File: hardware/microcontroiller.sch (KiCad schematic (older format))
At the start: 16 parts, among them J100 Conn_01x03, J2 Conn_02x03_Odd_Even, J3 USB_A, SW1 RESET Switch, U1 STM32L4Q5xx, Y1 32.768kHz

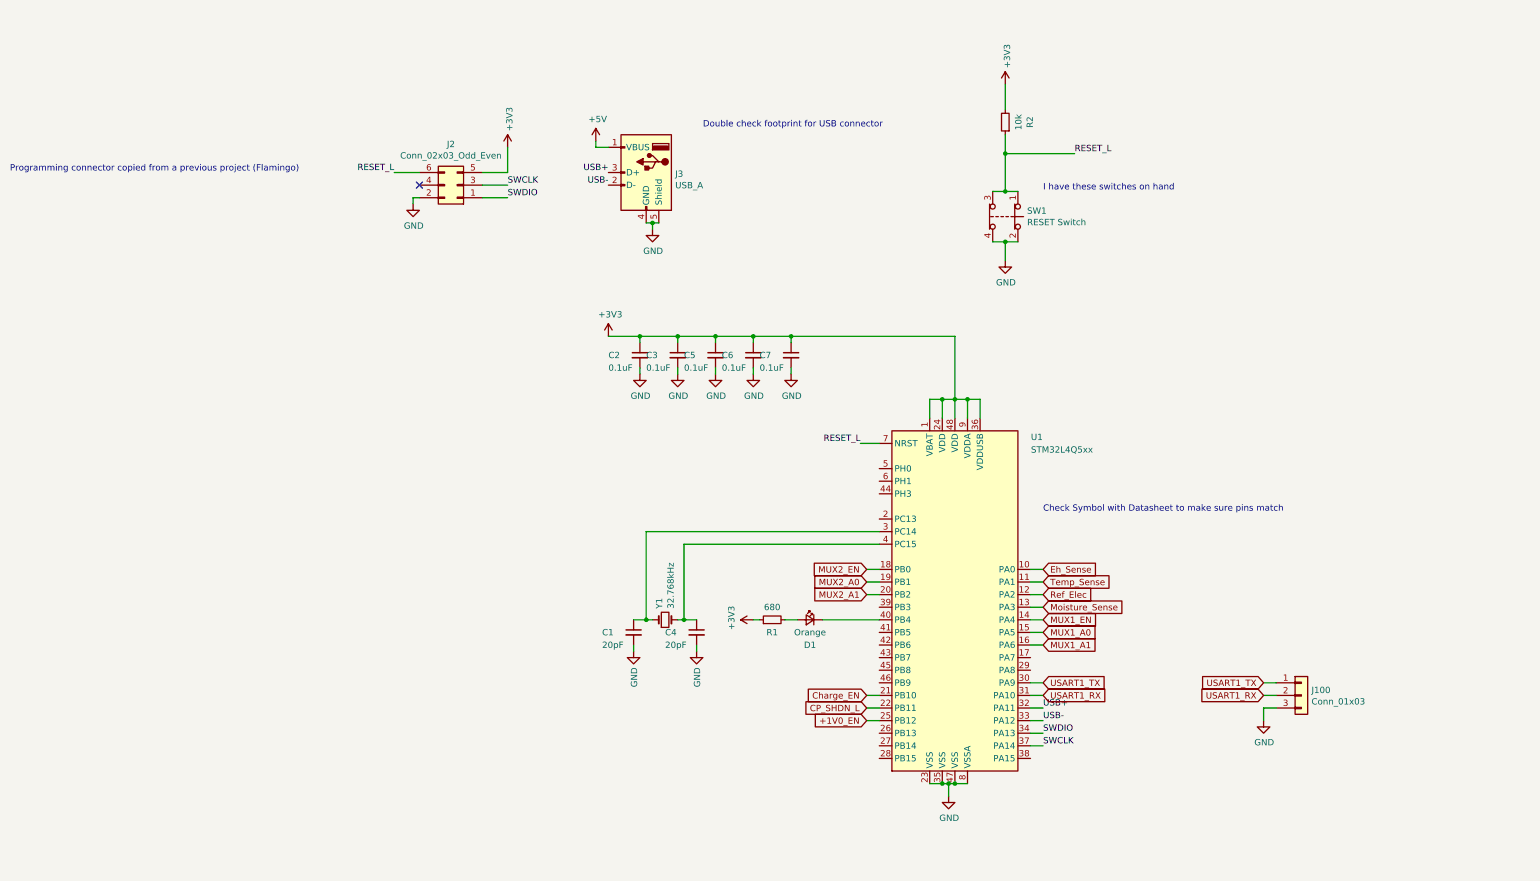
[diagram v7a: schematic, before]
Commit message: Updated footprint and added decoupling caps
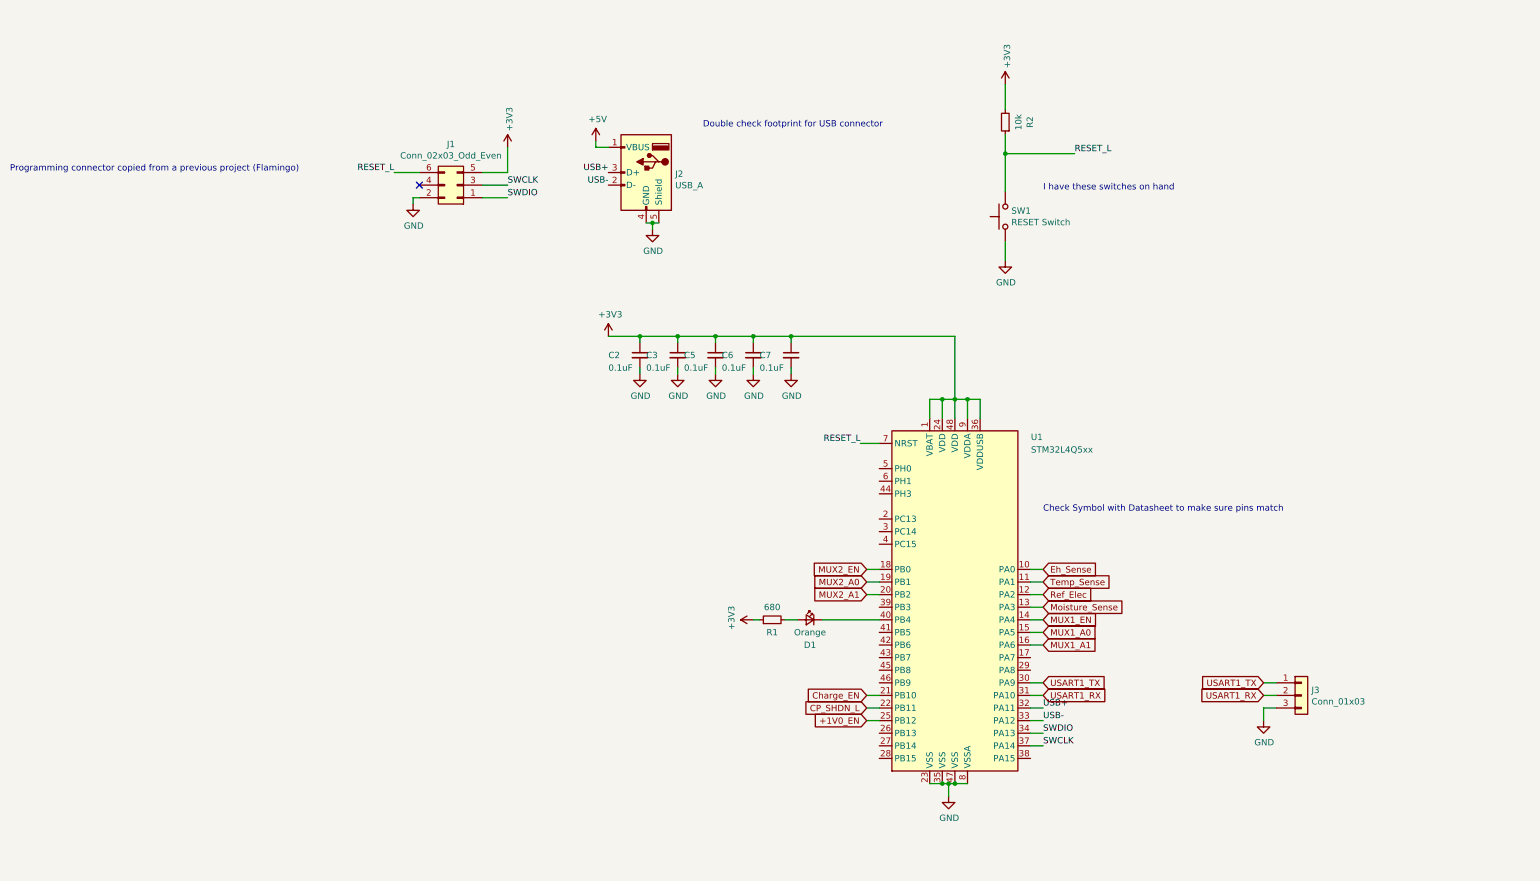
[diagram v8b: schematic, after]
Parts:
- removed C1, C4: 20pF, Capacitor_SMD:C_0603_1608Metric_Pad1.08x0.95mm_HandSolder, symbol mallard-rescue:C_Small-Device
- removed SW1: RESET Switch, Button_Switch_SMD:SW_SPST_B3U-1000P, symbol mallard-rescue:SW_Push_Open_Dual-Switch
- removed Y1: 32.768kHz, symbol mallard-rescue:Crystal_Small-Device
- added SW1: RESET Switch, Button_Switch_SMD:SW_SPST_B3U-1000P, symbol Switch:SW_Push
- renumbered J2 to J1, J3 to J2, J100 to J3
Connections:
- net GND: now also SW1.1
- net RESET_L: now also SW1.2
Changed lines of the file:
@@
 $Descr A4 11693 8268
 encoding utf-8
-Sheet 1 1
+Sheet 2 4
 Title ""
 Date ""
@@
 $EndDescr
 $Comp
-L mallard-rescue:+3V3-power #PWR07
+L mallard-rescue:+3V3-power #PWR04
 U 1 1 6157176B
 P 3200 3100
-F 0 "#PWR07" H 3200 2950 50  0001 C CNN
+F 0 "#PWR04" H 3200 2950 50  0001 C CNN
 F 1 "+3V3" H 3215 3273 50  0000 C CNN
 F 2 "" H 3200 3100 50  0001 C CNN
@@
 	6350 1300 6350 1100
 $Comp
-L mallard-rescue:+3V3-power #PWR018
+L mallard-rescue:+3V3-power #PWR015
 U 1 1 6157E7E5
 P 6350 1100
-F 0 "#PWR018" H 6350 950 50  0001 C CNN
+F 0 "#PWR015" H 6350 950 50  0001 C CNN
 F 1 "+3V3" V 6365 1228 50  0000 L CNN
 F 2 "" H 6350 1100 50  0001 C CNN
@@
 $EndComp
 $Comp
-L mallard-rescue:GND-power #PWR019
+L mallard-rescue:GND-power #PWR016
 U 1 1 615824DA
 P 6350 2500
-F 0 "#PWR019" H 6350 2250 50  0001 C CNN
+F 0 "#PWR016" H 6350 2250 50  0001 C CNN
 F 1 "GND" H 6355 2327 50  0000 C CNN
 F 2 "" H 6350 2500 50  0001 C CNN
@@
 Wire Wire Line
 	5350 3950 5200 3950
-$Comp
-L mallard-rescue:Crystal_Small-Device Y1
-U 1 1 6158BC98
-P 3650 5350
-F 0 "Y1" V 3604 5438 50  0000 L CNN
-F 1 "32.768kHz" V 3695 5438 50  0000 L CNN
-F 2 "" H 3650 5350 50  0001 C CNN
-F 3 "~" H 3650 5350 50  0001 C CNN
-	1    3650 5350
-	1    0    0    -1
-$EndComp
-$Comp
-L mallard-rescue:C_Small-Device C1
-U 1 1 6158E0B8
-P 3400 5450
-F 0 "C1" H 3150 5450 50  0000 L CNN
-F 1 "20pF" H 3150 5350 50  0000 L CNN
-F 2 "Capacitor_SMD:C_0603_1608Metric_Pad1.08x0.95mm_HandSolder" H 3400 5450 50  0001 C CNN
-F 3 "https://content.kemet.com/datasheets/KEM_C1007_X8R_ULTRA_150C_SMD.pdf" H 3400 5450 50  0001 C CNN
-F 4 "399-C0603C200G4HAC7867CT-ND" H 3400 5450 50  0001 C CNN "Digikey"
-	1    3400 5450
-	1    0    0    -1
-$EndComp
-$Comp
-L mallard-rescue:GND-power #PWR08
-U 1 1 6158FD84
-P 3400 5600
-F 0 "#PWR08" H 3400 5350 50  0001 C CNN
-F 1 "GND" V 3405 5472 50  0000 R CNN
-F 2 "" H 3400 5600 50  0001 C CNN
-F 3 "" H 3400 5600 50  0001 C CNN
-	1    3400 5600
-	1    0    0    -1
-$EndComp
 Text Notes 6650 4500 0    50   ~ 0
 Check Symbol with Datasheet to make sure pins match
@@
 Connection ~ 5900 6650
 $Comp
-L mallard-rescue:GND-power #PWR017
+L mallard-rescue:GND-power #PWR014
 U 1 1 616159A6
 P 5900 6750
-F 0 "#PWR017" H 5900 6500 50  0001 C CNN
+F 0 "#PWR014" H 5900 6500 50  0001 C CNN
 F 1 "GND" H 5905 6577 50  0000 C CNN
 F 2 "" H 5900 6750 50  0001 C CNN
@@
 $EndComp
 $Comp
-L mallard-rescue:USB_A-Connector J?
+L mallard-rescue:USB_A-Connector J2
 U 1 1 6161D470
 P 3500 1800
-AR Path="/6161D470" Ref="J?"  Part="1"
-AR Path="/60B3FDDE/6161D470" Ref="J3"  Part="1"
-F 0 "J3" H 3270 1789 50  0000 R CNN
+AR Path="/6161D470" Ref="J2"  Part="1"
+AR Path="/60B3FDDE/6161D470" Ref="J?"  Part="1"
+F 0 "J?" H 3270 1789 50  0000 R CNN
 F 1 "USB_A" H 3270 1698 50  0000 R CNN
 F 2 "Connector_USB:USB3_A_Molex_48393-001" H 3650 1750 50  0001 C CNN
@@
 $EndComp
 $Comp
-L mallard-rescue:+5V-power #PWR06
+L mallard-rescue:+5V-power #PWR03
 U 1 1 6162177A
 P 3100 1550
-F 0 "#PWR06" H 3100 1400 50  0001 C CNN
+F 0 "#PWR03" H 3100 1400 50  0001 C CNN
 F 1 "+5V" H 3115 1723 50  0000 C CNN
 F 2 "" H 3100 1550 50  0001 C CNN
@@
 USB-
 $Comp
-L mallard-rescue:GND-power #PWR010
+L mallard-rescue:GND-power #PWR07
 U 1 1 6162345E
 P 3550 2250
-F 0 "#PWR010" H 3550 2000 50  0001 C CNN
+F 0 "#PWR07" H 3550 2000 50  0001 C CNN
 F 1 "GND" H 3555 2077 50  0000 C CNN
 F 2 "" H 3550 2250 50  0001 C CNN
@@
 Wire Wire Line
 	3550 2200 3500 2200
-$Comp
-L mallard-rescue:SW_Push_Open_Dual-Switch SW1
-U 1 1 6162FC27
-P 6450 2150
-F 0 "SW1" V 6404 2223 50  0000 L CNN
-F 1 "RESET Switch" V 6495 2223 50  0000 L CNN
-F 2 "Button_Switch_SMD:SW_SPST_B3U-1000P" H 6450 2350 50  0001 C CNN
-F 3 "https://omronfs.omron.com/en_US/ecb/products/pdf/en-b3u.pdf" H 6450 2350 50  0001 C CNN
-F 4 "SW1020CT-ND" H 6450 2150 50  0001 C CNN "Digikey"
-	1    6450 2150
-	0    1    1    0
-$EndComp
-Wire Wire Line
-	6250 2350 6350 2350
-Connection ~ 6350 2350
-Wire Wire Line
-	6350 2350 6450 2350
 Wire Wire Line
 	6350 2350 6350 2500
-Wire Wire Line
-	6250 1950 6350 1950
-Connection ~ 6350 1950
-Wire Wire Line
-	6350 1950 6450 1950
 $Comp
 L mallard-rescue:LED_Small-Device D1
@@
 	4600 5350 4700 5350
 $Comp
-L mallard-rescue:+3V3-power #PWR015
+L mallard-rescue:+3V3-power #PWR012
 U 1 1 61652B46
 P 4350 5350
-F 0 "#PWR015" H 4350 5200 50  0001 C CNN
+F 0 "#PWR012" H 4350 5200 50  0001 C CNN
 F 1 "+3V3" H 4365 5523 50  0000 C CNN
 F 2 "" H 4350 5350 50  0001 C CNN
@@
 	5250 6150 5350 6150
 $Comp
-L mallard-rescue:GND-power #PWR09
+L mallard-rescue:GND-power #PWR06
 U 1 1 615C81D2
 P 3450 3400
-F 0 "#PWR09" H 3450 3150 50  0001 C CNN
+F 0 "#PWR06" H 3450 3150 50  0001 C CNN
 F 1 "GND" H 3455 3227 50  0000 C CNN
 F 2 "" H 3450 3400 50  0001 C CNN
@@
 Connection ~ 4050 3100
 $Comp
-L mallard-rescue:GND-power #PWR011
+L mallard-rescue:GND-power #PWR08
 U 1 1 61A5AA42
 P 3750 3400
-F 0 "#PWR011" H 3750 3150 50  0001 C CNN
+F 0 "#PWR08" H 3750 3150 50  0001 C CNN
 F 1 "GND" H 3755 3227 50  0000 C CNN
 F 2 "" H 3750 3400 50  0001 C CNN
@@
 $EndComp
 $Comp
-L mallard-rescue:GND-power #PWR013
+L mallard-rescue:GND-power #PWR010
 U 1 1 61A5C967
 P 4050 3400
-F 0 "#PWR013" H 4050 3150 50  0001 C CNN
+F 0 "#PWR010" H 4050 3150 50  0001 C CNN
 F 1 "GND" H 4055 3227 50  0000 C CNN
 F 2 "" H 4050 3400 50  0001 C CNN
@@
 $EndComp
 $Comp
-L mallard-rescue:GND-power #PWR014
+L mallard-rescue:GND-power #PWR011
 U 1 1 61A5E793
 P 4350 3400
-F 0 "#PWR014" H 4350 3150 50  0001 C CNN
+F 0 "#PWR011" H 4350 3150 50  0001 C CNN
 F 1 "GND" H 4355 3227 50  0000 C CNN
 F 2 "" H 4350 3400 50  0001 C CNN
@@
 $EndComp
 $Comp
-L mallard-rescue:GND-power #PWR016
+L mallard-rescue:GND-power #PWR013
 U 1 1 61A60A8A
 P 4650 3400
-F 0 "#PWR016" H 4650 3150 50  0001 C CNN
+F 0 "#PWR013" H 4650 3150 50  0001 C CNN
 F 1 "GND" H 4655 3227 50  0000 C CNN
 F 2 "" H 4650 3400 50  0001 C CNN
@@
 Connection ~ 6050 3600
 $Comp
-L mallard-rescue:C_Small-Device C4
-U 1 1 61A825EB
-P 3900 5450
-F 0 "C4" H 3650 5450 50  0000 L CNN
-F 1 "20pF" H 3650 5350 50  0000 L CNN
-F 2 "Capacitor_SMD:C_0603_1608Metric_Pad1.08x0.95mm_HandSolder" H 3900 5450 50  0001 C CNN
-F 3 "https://content.kemet.com/datasheets/KEM_C1007_X8R_ULTRA_150C_SMD.pdf" H 3900 5450 50  0001 C CNN
-F 4 "399-C0603C200G4HAC7867CT-ND" H 3900 5450 50  0001 C CNN "Digikey"
-	1    3900 5450
-	1    0    0    -1
-$EndComp
-$Comp
 L mallard-rescue:C_Small-Device C3
 U 1 1 61A86DBF
@@
 Text Notes 3950 1450 0    50   ~ 0
 Double check footprint for USB connector
-$Comp
-L mallard-rescue:GND-power #PWR012
-U 1 1 618D755A
-P 3900 5600
-F 0 "#PWR012" H 3900 5350 50  0001 C CNN
-F 1 "GND" V 3905 5472 50  0000 R CNN
-F 2 "" H 3900 5600 50  0001 C CNN
-F 3 "" H 3900 5600 50  0001 C CNN
-	1    3900 5600
-	1    0    0    -1
-$EndComp
-Wire Wire Line
-	3400 5600 3400 5550
-Wire Wire Line
-	3900 5600 3900 5550
-Wire Wire Line
-	3400 5350 3500 5350
-Wire Wire Line
-	3900 5350 3800 5350
-Wire Wire Line
-	3500 5350 3500 4650
-Wire Wire Line
-	3500 4650 5350 4650
-Connection ~ 3500 5350
-Wire Wire Line
-	3500 5350 3550 5350
-Wire Wire Line
-	3800 5350 3800 4750
-Wire Wire Line
-	3800 4750 5350 4750
-Connection ~ 3800 5350
-Wire Wire Line
-	3800 5350 3750 5350
 Wire Wire Line
 	6350 1500 6350 1650
@@
 Programming connector copied from a previous project (Flamingo)
 $Comp
-L Connector_Generic:Conn_02x03_Odd_Even J2
+L Connector_Generic:Conn_02x03_Odd_Even J1
 U 1 1 61EC204C
 P 2000 1900
-F 0 "J2" H 2050 1575 50  0000 C CNN
+F 0 "J1" H 2050 1575 50  0000 C CNN
 F 1 "Conn_02x03_Odd_Even" H 2050 1666 50  0000 C CNN
 F 2 "Connector_PinHeader_1.27mm:PinHeader_2x03_P1.27mm_Vertical" H 2000 1900 50  0001 C CNN
@@
 	1650 2000 1650 2050
 $Comp
-L mallard-rescue:GND-power #PWR04
+L mallard-rescue:GND-power #PWR01
 U 1 1 61ECF0E0
 P 1650 2050
-F 0 "#PWR04" H 1650 1800 50  0001 C CNN
+F 0 "#PWR01" H 1650 1800 50  0001 C CNN
 F 1 "GND" H 1655 1877 50  0000 C CNN
 F 2 "" H 1650 2050 50  0001 C CNN
@@
 $EndComp
 $Comp
-L mallard-rescue:+3V3-power #PWR05
+L mallard-rescue:+3V3-power #PWR02
 U 1 1 61ED1EE0
 P 2400 1600
-F 0 "#PWR05" H 2400 1450 50  0001 C CNN
+F 0 "#PWR02" H 2400 1450 50  0001 C CNN
 F 1 "+3V3" V 2415 1728 50  0000 L CNN
 F 2 "" H 2400 1600 50  0001 C CNN
@@
 	8500 5850 8400 5850
 $Comp
-L Connector_Generic:Conn_01x03 J100
+L Connector_Generic:Conn_01x03 J3
 U 1 1 61EA675F
 P 8700 5950
-F 0 "J100" H 8780 5992 50  0000 L CNN
+F 0 "J3" H 8780 5992 50  0000 L CNN
 F 1 "Conn_01x03" H 8780 5901 50  0000 L CNN
 F 2 "Connector_PinHeader_2.54mm:PinHeader_1x03_P2.54mm_Vertical_SMD_Pin1Right" H 8700 5950 50  0001 C CNN
@@
 	8400 6050 8400 6150
 $Comp
-L mallard-rescue:GND-power #PWR?
+L mallard-rescue:GND-power #PWR017
 U 1 1 61EAAB16
 P 8400 6150
-F 0 "#PWR?" H 8400 5900 50  0001 C CNN
+F 0 "#PWR017" H 8400 5900 50  0001 C CNN
 F 1 "GND" H 8405 5977 50  0000 C CNN
 F 2 "" H 8400 6150 50  0001 C CNN
@@
 Wire Wire Line
 	8500 6050 8400 6050
+$Comp
+L Switch:SW_Push SW1
+U 1 1 61ECF5F6
+P 6350 2150
+F 0 "SW1" V 6396 2102 50  0000 R CNN
+F 1 "RESET Switch" V 6305 2102 50  0000 R CNN
+F 2 "Button_Switch_SMD:SW_SPST_B3U-1000P" H 6350 2350 50  0001 C CNN
+F 3 "https://omronfs.omron.com/en_US/ecb/products/pdf/en-b3u.pdf" H 6350 2350 50  0001 C CNN
+F 4 "SW1020CT-ND" V 6350 2150 50  0001 C CNN "Digikey"
+	1    6350 2150
+	0    -1   -1   0
+$EndComp
 $EndSCHEMATC
